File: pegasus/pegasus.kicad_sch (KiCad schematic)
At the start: 30 parts, among them IC2 RFD900ux-SMT, IC3 L70B-M39, J1 Screw_Terminal_01x04, J2 Screw_Terminal_01x02, Q1 BC817, U1 Teensy4.0, U2 CON-SMA-EDGE-S, U3 CON-SMA-EDGE-S, U4 XTSD04GCLGEGA, U5 AZ1117-ADJ

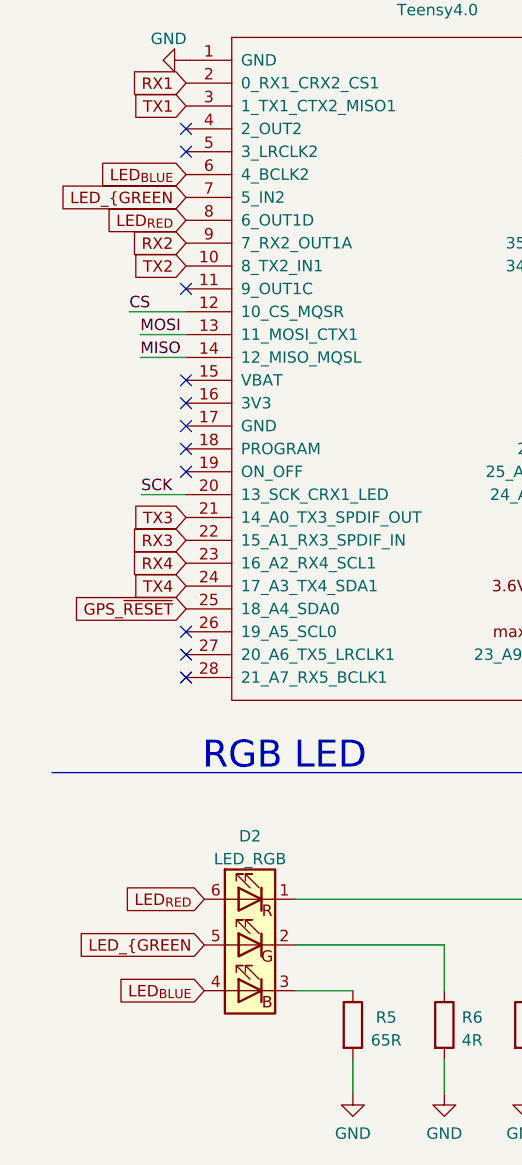
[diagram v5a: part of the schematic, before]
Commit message: change LED pin names to reflect proper colors
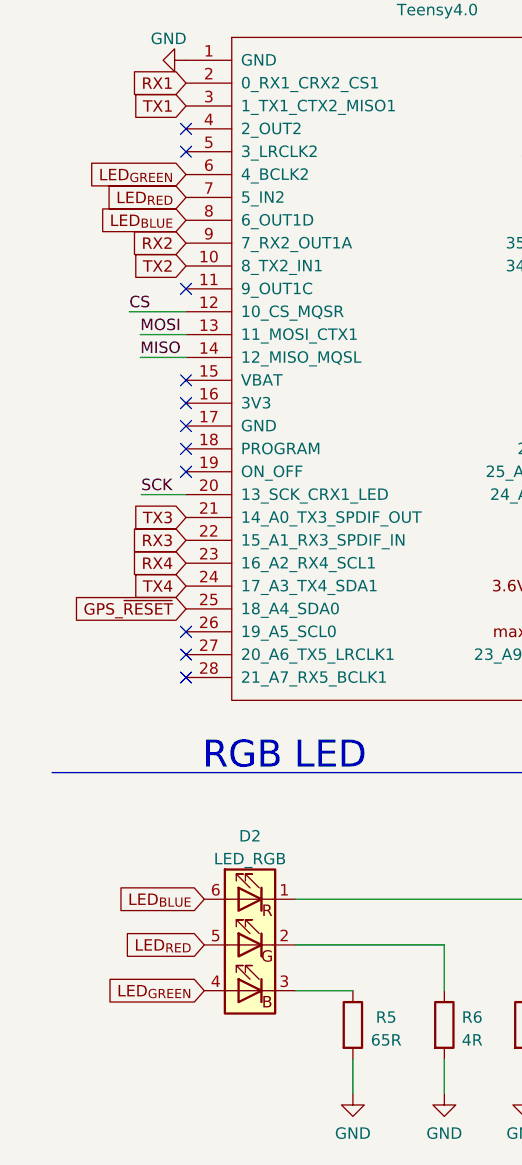
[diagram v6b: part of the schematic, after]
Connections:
- net LED_{GREEN is gone; now on net LED_{RED}: D2.5 (GA), U1.7 (5_IN2)
- net LED_{BLUE}: now also D2.6 (RA), U1.8 (6_OUT1D); no longer D2.4 (BA), U1.6 (4_BCLK2)
- net LED_{RED}: no longer D2.6 (RA), U1.8 (6_OUT1D)
- new net LED_{GREEN}: D2.4 (BA), U1.6 (4_BCLK2)
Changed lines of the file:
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@@
     (effects (font (size 1.27 1.27)) (justify left bottom))
   )
-  (global_label "LED_{GREEN" (shape input) (at 27.178 90.932 180) (fields_autoplaced)
+  (global_label "LED_{RED}" (shape input) (at 27.178 90.932 180) (fields_autoplaced)
     (effects (font (size 1.27 1.27)) (justify right))
-    (property "Intersheet References" "${INTERSHEET_REFS}" (id 0) (at 16.3829 90.8526 0)
+    (property "Intersheet References" "${INTERSHEET_REFS}" (id 0) (at 18.3665 90.8526 0)
       (effects (font (size 1.27 1.27)) (justify right) hide)
     )
   )
-  (global_label "LED_{BLUE}" (shape input) (at 29.21 179.07 180) (fields_autoplaced)
+  (global_label "LED_{GREEN}" (shape input) (at 29.21 179.07 180) (fields_autoplaced)
     (effects (font (size 1.27 1.27)) (justify right))
-    (property "Intersheet References" "${INTERSHEET_REFS}" (id 0) (at 19.5277 178.9906 0)
+    (property "Intersheet References" "${INTERSHEET_REFS}" (id 0) (at 18.4149 178.9906 0)
       (effects (font (size 1.27 1.27)) (justify right) hide)
     )
@@
     )
   )
-  (global_label "LED_{RED}" (shape input) (at 27.178 93.472 180) (fields_autoplaced)
+  (global_label "LED_{BLUE}" (shape input) (at 27.178 93.472 180) (fields_autoplaced)
     (effects (font (size 1.27 1.27)) (justify right))
-    (property "Intersheet References" "${INTERSHEET_REFS}" (id 0) (at 18.3665 93.3926 0)
+    (property "Intersheet References" "${INTERSHEET_REFS}" (id 0) (at 17.4957 93.3926 0)
       (effects (font (size 1.27 1.27)) (justify right) hide)
     )
@@
     )
   )
-  (global_label "LED_{RED}" (shape input) (at 29.21 168.91 180) (fields_autoplaced)
+  (global_label "LED_{BLUE}" (shape input) (at 29.21 168.91 180) (fields_autoplaced)
     (effects (font (size 1.27 1.27)) (justify right))
-    (property "Intersheet References" "${INTERSHEET_REFS}" (id 0) (at 20.3985 168.8306 0)
+    (property "Intersheet References" "${INTERSHEET_REFS}" (id 0) (at 19.5277 168.8306 0)
       (effects (font (size 1.27 1.27)) (justify right) hide)
     )
   )
-  (global_label "LED_{GREEN" (shape input) (at 29.21 173.99 180) (fields_autoplaced)
+  (global_label "LED_{RED}" (shape input) (at 29.21 173.99 180) (fields_autoplaced)
     (effects (font (size 1.27 1.27)) (justify right))
-    (property "Intersheet References" "${INTERSHEET_REFS}" (id 0) (at 18.4149 173.9106 0)
+    (property "Intersheet References" "${INTERSHEET_REFS}" (id 0) (at 20.3985 173.9106 0)
       (effects (font (size 1.27 1.27)) (justify right) hide)
     )
@@
     )
   )
-  (global_label "LED_{BLUE}" (shape input) (at 27.178 88.392 180) (fields_autoplaced)
+  (global_label "LED_{GREEN}" (shape input) (at 27.178 88.392 180) (fields_autoplaced)
     (effects (font (size 1.27 1.27)) (justify right))
-    (property "Intersheet References" "${INTERSHEET_REFS}" (id 0) (at 17.4957 88.3126 0)
+    (property "Intersheet References" "${INTERSHEET_REFS}" (id 0) (at 16.3829 88.3126 0)
       (effects (font (size 1.27 1.27)) (justify right) hide)
     )
